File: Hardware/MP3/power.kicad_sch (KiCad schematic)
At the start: 31 parts, among them IC1 MCP73871-2CCI_ML, U1 TPS63000DRCR, U3 TPS7A20xxxDQN, U4 TPS7A20xxxDQN, U6 TPS7A20xxxDQN

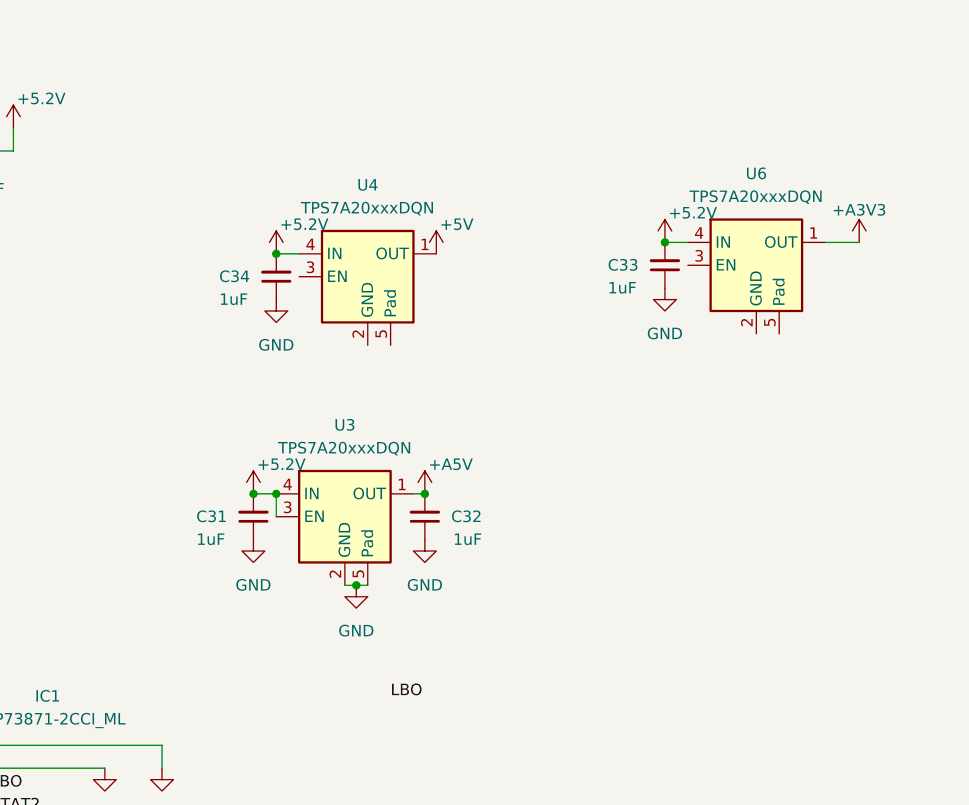
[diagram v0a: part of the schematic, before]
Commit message: feat: Changes to the power circuitry to sort out the regulators (schematic and footprint sorted). Additionally, headphone jack needs to be sorted, both schematic and actual component.
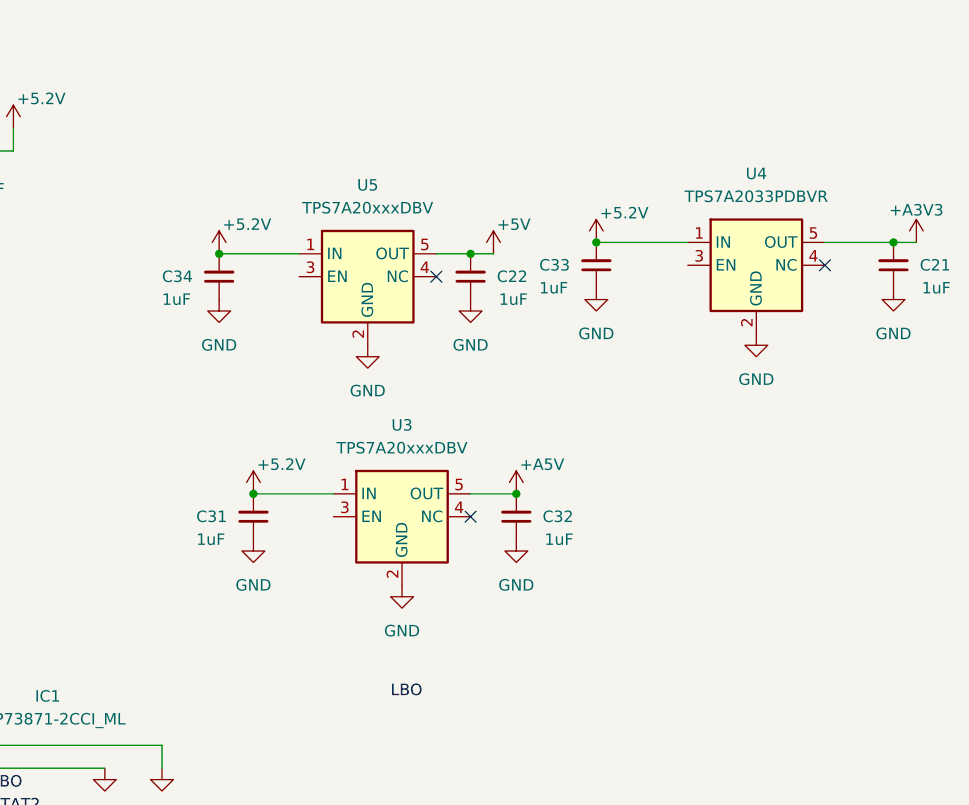
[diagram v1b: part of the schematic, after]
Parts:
- removed U3: TPS7A20xxxDQN, Package_TO_SOT_SMD:SOT-23-5, symbol Regulator_Linear:TPS7A20xxxDQN
- removed U4, U6: TPS7A20xxxDQN, Package_SON:Texas_X2SON-4_1x1mm_P0.65mm, symbol Regulator_Linear:TPS7A20xxxDQN
- added C21, C22: 1uF, Capacitor_SMD:C_0402_1005Metric, symbol Device:C_Small
- added U3, U5: TPS7A20xxxDBV, Package_TO_SOT_SMD:SOT-23-5, symbol Library:TPS7A20xxxDBV
- added U4: TPS7A2033PDBVR, Package_TO_SOT_SMD:SOT-23-5, symbol Library:TPS7A20xxxDBV
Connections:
- net +5.2V: now also U3.1 (IN), U4.1 (IN), U5.1 (IN)
- net +5V: now also C22.2, U5.5 (OUT)
- net +A3V3: now also C21.2, U4.5 (OUT)
- net +A5V: now also U3.5 (OUT)
- net GND: now also C21.1, C22.1, U3.2 (GND), U4.2 (GND), U5.2 (GND)
- no-connect marks 0 -> 3
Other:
- moved on the sheet: C32, C33, C34
